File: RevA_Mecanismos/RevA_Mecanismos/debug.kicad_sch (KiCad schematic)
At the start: 2 parts

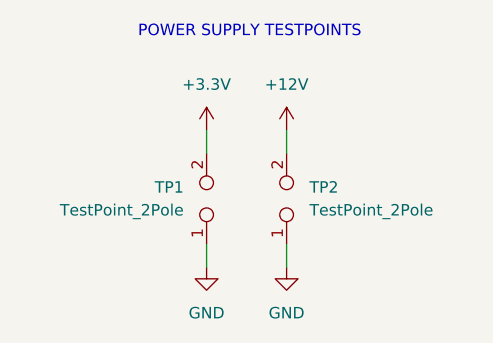
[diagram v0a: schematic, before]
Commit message: Added H-Bridges and voltage regulators
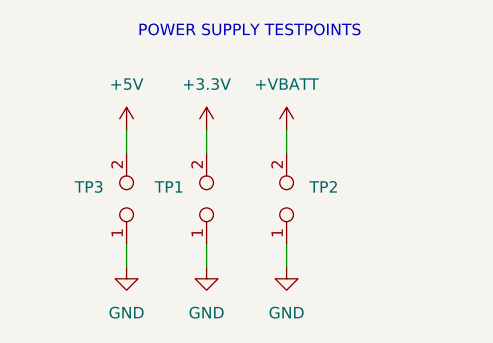
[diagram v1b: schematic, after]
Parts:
- added TP3: TestPoint_2Pole, TestPoint:TestPoint_2Pads_Pitch5.08mm_Drill1.3mm, symbol Connector:TestPoint_2Pole
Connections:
- net GND: now also TP3.1
- net +12V renamed +VMOT
- new net +5V: TP3.2
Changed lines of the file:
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@@
 (kicad_sch (version 20230121) (generator eeschema)
   (paper "A4")
+  (wire (pts (xy 218.44 134.62) (xy 218.44 132.08))
+    (stroke (width 0) (type solid))
+  )
   (wire (pts (xy 236.22 134.62) (xy 236.22 132.08))
     (stroke (width 0) (type default))
@@
     (stroke (width 0) (type solid))
   )
+  (wire (pts (xy 218.44 147.32) (xy 218.44 144.78))
+    (stroke (width 0) (type solid))
+  )
   (wire (pts (xy 236.22 147.32) (xy 236.22 144.78))
     (stroke (width 0) (type solid))
@@
     (effects (font (size 1.27 1.27)) (justify left bottom))
   )
+  (symbol (lib_id "CustomUtilities:+VBATT") (at 236.22 132.08 0) (unit 1)
+    (in_bom yes) (on_board yes) (dnp no)
+    (property "Reference" "#PWR054" (at 236.22 132.08 0)
+      (effects (font (size 1.27 1.27)) hide)
+    )
+    (property "Value" "+VBATT" (at 236.22 127 0)
+      (effects (font (size 1.27 1.27)))
+    )
+    (property "Footprint" "" (at 236.22 132.08 0)
+      (effects (font (size 1.27 1.27)) hide)
+    )
+    (property "Datasheet" "" (at 236.22 132.08 0)
+      (effects (font (size 1.27 1.27)) hide)
+    )
+    (pin "1")
+    (instances
+      (project "RevA_Mecanismos"
+        (path "/3a16a434-10b7-49a8-988b-273362cb395e/9466c5e7-8595-42d4-852d-e47b24624149"
+          (reference "#PWR054") (unit 1)
+        )
+        (path "/3a16a434-10b7-49a8-988b-273362cb395e/a0534dee-4bf0-4ee7-89a4-28a5c95a5477"
+          (reference "#PWR030") (unit 1)
+        )
+      )
+    )
+  )
   (symbol (lib_id "power:GND") (at 227.33 147.32 0) (unit 1)
     (in_bom yes) (on_board yes) (dnp no)
@@
         (path "/6afa037b-8727-4bf3-bca2-b74b900c310e/e4c969ea-19dc-43d6-ab23-93022e90983a"
           (reference "#PWR0170") (unit 1)
+        )
+      )
+    )
+  )
+  (symbol (lib_id "Connector:TestPoint_2Pole") (at 218.44 139.7 90) (unit 1)
+    (in_bom yes) (on_board yes) (dnp no)
+    (property "Reference" "TP3" (at 215.9 138.43 90)
+      (effects (font (size 1.27 1.27)) (justify left))
+    )
+    (property "Value" "TestPoint_2Pole" (at 215.9 140.97 90)
+      (effects (font (size 1.27 1.27)) (justify left) hide)
+    )
+    (property "Footprint" "TestPoint:TestPoint_2Pads_Pitch5.08mm_Drill1.3mm" (at 218.44 139.7 0)
+      (effects (font (size 1.27 1.27)) hide)
+    )
+    (property "Datasheet" "~" (at 218.44 139.7 0)
+      (effects (font (size 1.27 1.27)) hide)
+    )
+    (pin "1")
+    (pin "2")
+    (instances
+      (project "RevA_Mecanismos"
+        (path "/3a16a434-10b7-49a8-988b-273362cb395e/a0534dee-4bf0-4ee7-89a4-28a5c95a5477"
+          (reference "TP3") (unit 1)
+        )
+      )
+      (project "IO_module"
+        (path "/6afa037b-8727-4bf3-bca2-b74b900c310e/e4c969ea-19dc-43d6-ab23-93022e90983a"
+          (reference "TP3") (unit 1)
         )
       )
@@
     )
     (property "Value" "TestPoint_2Pole" (at 238.76 140.97 90)
-      (effects (font (size 1.27 1.27)) (justify right))
+      (effects (font (size 1.27 1.27)) (justify right) hide)
     )
     (property "Footprint" "TestPoint:TestPoint_2Pads_Pitch5.08mm_Drill1.3mm" (at 236.22 139.7 0)
@@
     )
   )
-  (symbol (lib_id "power:+12V") (at 236.22 132.08 0) (unit 1)
-    (in_bom yes) (on_board yes) (dnp no)
-    (property "Reference" "#PWR030" (at 236.22 135.89 0)
-      (effects (font (size 1.27 1.27)) hide)
-    )
-    (property "Value" "+12V" (at 236.22 127 0)
-      (effects (font (size 1.27 1.27)))
-    )
-    (property "Footprint" "" (at 236.22 132.08 0)
-      (effects (font (size 1.27 1.27)) hide)
-    )
-    (property "Datasheet" "" (at 236.22 132.08 0)
-      (effects (font (size 1.27 1.27)) hide)
-    )
-    (pin "1")
-    (instances
-      (project "RevA_Mecanismos"
-        (path "/3a16a434-10b7-49a8-988b-273362cb395e/a0534dee-4bf0-4ee7-89a4-28a5c95a5477"
-          (reference "#PWR030") (unit 1)
-        )
-      )
-      (project "IO_module"
-        (path "/6afa037b-8727-4bf3-bca2-b74b900c310e/e4c969ea-19dc-43d6-ab23-93022e90983a"
-          (reference "#PWR0172") (unit 1)
-        )
-      )
-    )
-  )
   (symbol (lib_id "power:GND") (at 236.22 147.32 0) (unit 1)
     (in_bom yes) (on_board yes) (dnp no)
@@
         (path "/6afa037b-8727-4bf3-bca2-b74b900c310e/e4c969ea-19dc-43d6-ab23-93022e90983a"
           (reference "#PWR0171") (unit 1)
+        )
+      )
+    )
+  )
+  (symbol (lib_id "power:GND") (at 218.44 147.32 0) (unit 1)
+    (in_bom yes) (on_board yes) (dnp no)
+    (property "Reference" "#PWR057" (at 218.44 153.67 0)
+      (effects (font (size 1.27 1.27)) hide)
+    )
+    (property "Value" "GND" (at 218.44 152.4 0)
+      (effects (font (size 1.27 1.27)))
+    )
+    (property "Footprint" "" (at 218.44 147.32 0)
+      (effects (font (size 1.27 1.27)) hide)
+    )
+    (property "Datasheet" "" (at 218.44 147.32 0)
+      (effects (font (size 1.27 1.27)) hide)
+    )
+    (pin "1")
+    (instances
+      (project "RevA_Mecanismos"
+        (path "/3a16a434-10b7-49a8-988b-273362cb395e/a0534dee-4bf0-4ee7-89a4-28a5c95a5477"
+          (reference "#PWR057") (unit 1)
+        )
+      )
+      (project "IO_module"
+        (path "/6afa037b-8727-4bf3-bca2-b74b900c310e/e4c969ea-19dc-43d6-ab23-93022e90983a"
+          (reference "#PWR0170") (unit 1)
+        )
+      )
+    )
+  )
+  (symbol (lib_id "power:+5V") (at 218.44 132.08 0) (unit 1)
+    (in_bom yes) (on_board yes) (dnp no)
+    (property "Reference" "#PWR056" (at 218.44 135.89 0)
+      (effects (font (size 1.27 1.27)) hide)
+    )
+    (property "Value" "+5V" (at 218.44 127 0)
+      (effects (font (size 1.27 1.27)))
+    )
+    (property "Footprint" "" (at 218.44 132.08 0)
+      (effects (font (size 1.27 1.27)) hide)
+    )
+    (property "Datasheet" "" (at 218.44 132.08 0)
+      (effects (font (size 1.27 1.27)) hide)
+    )
+    (pin "1")
+    (instances
+      (project "RevA_Mecanismos"
+        (path "/3a16a434-10b7-49a8-988b-273362cb395e/9466c5e7-8595-42d4-852d-e47b24624149"
+          (reference "#PWR056") (unit 1)
+        )
+        (path "/3a16a434-10b7-49a8-988b-273362cb395e/a0534dee-4bf0-4ee7-89a4-28a5c95a5477"
+          (reference "#PWR055") (unit 1)
+        )
+      )
+      (project "stepper_module_v2"
+        (path "/60aa52ba-7ce7-4ce8-b294-2b47b8740a05/e3d003d9-3702-47a9-9630-ba886331ecbf"
+          (reference "#PWR0141") (unit 1)
         )
       )
@@
     )
     (property "Value" "TestPoint_2Pole" (at 224.79 140.97 90)
-      (effects (font (size 1.27 1.27)) (justify left))
+      (effects (font (size 1.27 1.27)) (justify left) hide)
     )
     (property "Footprint" "TestPoint:TestPoint_2Pads_Pitch5.08mm_Drill1.3mm" (at 227.33 139.7 0)

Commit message: Created PCB project
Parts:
- added D13, D14, D15, D16, D17, D18: LED_Small, LED_SMD:LED_0603_1608Metric, symbol Device:LED_Small
- added J5: DEBUG_CONN, Connector_FFC-FPC:Hirose_FH12-24S-0.5SH_1x24-1MP_P0.50mm_Horizontal, symbol Connector:Conn_01x24_Pin
- added R21, R22, R23, R24, R25, R26: 220, Resistor_SMD:R_0603_1608Metric, symbol Device:R_Small
- added TP4: TestPoint_2Pole, TestPoint:TestPoint_2Pads_Pitch5.08mm_Drill1.3mm, symbol Connector:TestPoint_2Pole
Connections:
- net +3.3V: now also J5.24 (Pin_24)
- net GND: now also J5.22 (Pin_22), J5.23 (Pin_23), R21.2, R22.2, R23.2, R24.2, R25.2, R26.2
- new net: D18.1 (K), R26.1
- new net: D14.1 (K), R22.1
- new net: D17.1 (K), R25.1
- new net: D15.1 (K), R23.1
- new net: D13.1 (K), R21.1
- new net: D16.1 (K), R24.1
- new net CAN_RX: J5.18 (Pin_18), TP4.1
- new net CAN_TX: J5.19 (Pin_19), TP4.2
- new net DEBUG_1: D13.2 (A), J5.1 (Pin_1)
- new net DEBUG_2: D14.2 (A), J5.2 (Pin_2)
- new net DEBUG_3: D15.2 (A), J5.3 (Pin_3)
- new net DEBUG_4: D16.2 (A), J5.4 (Pin_4)
- new net DEBUG_5: D17.2 (A), J5.5 (Pin_5)
- new net DEBUG_6: D18.2 (A), J5.6 (Pin_6)
- new net SCL: J5.15 (Pin_15)
- new net SDA: J5.14 (Pin_14)
- new net UART_RX: J5.21 (Pin_21)
- new net UART_TX: J5.20 (Pin_20)
- no-connect marks 0 -> 9
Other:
- note added: "CANBUS TESTPOINTS"
- note added: "DEBUG CONNECTOR"
- note added: "DEBUG LEDS"
- note added: "Debug"
- note added: "FH12-24S-0.5SH(55)"

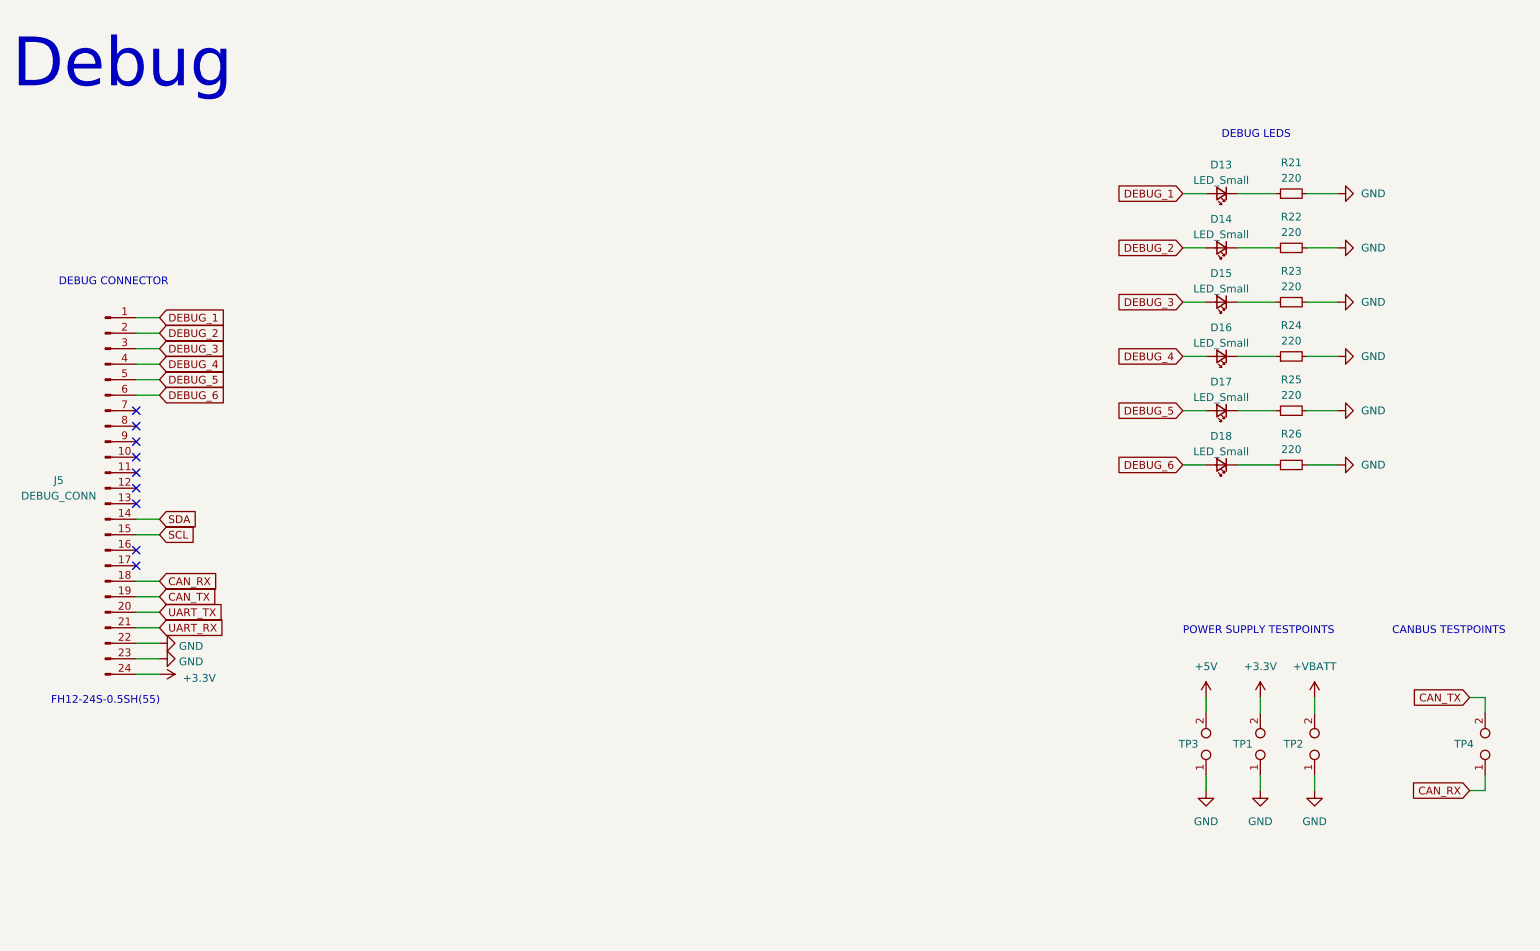
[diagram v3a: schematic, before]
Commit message: Updated STM32 USV Mechanism PCB
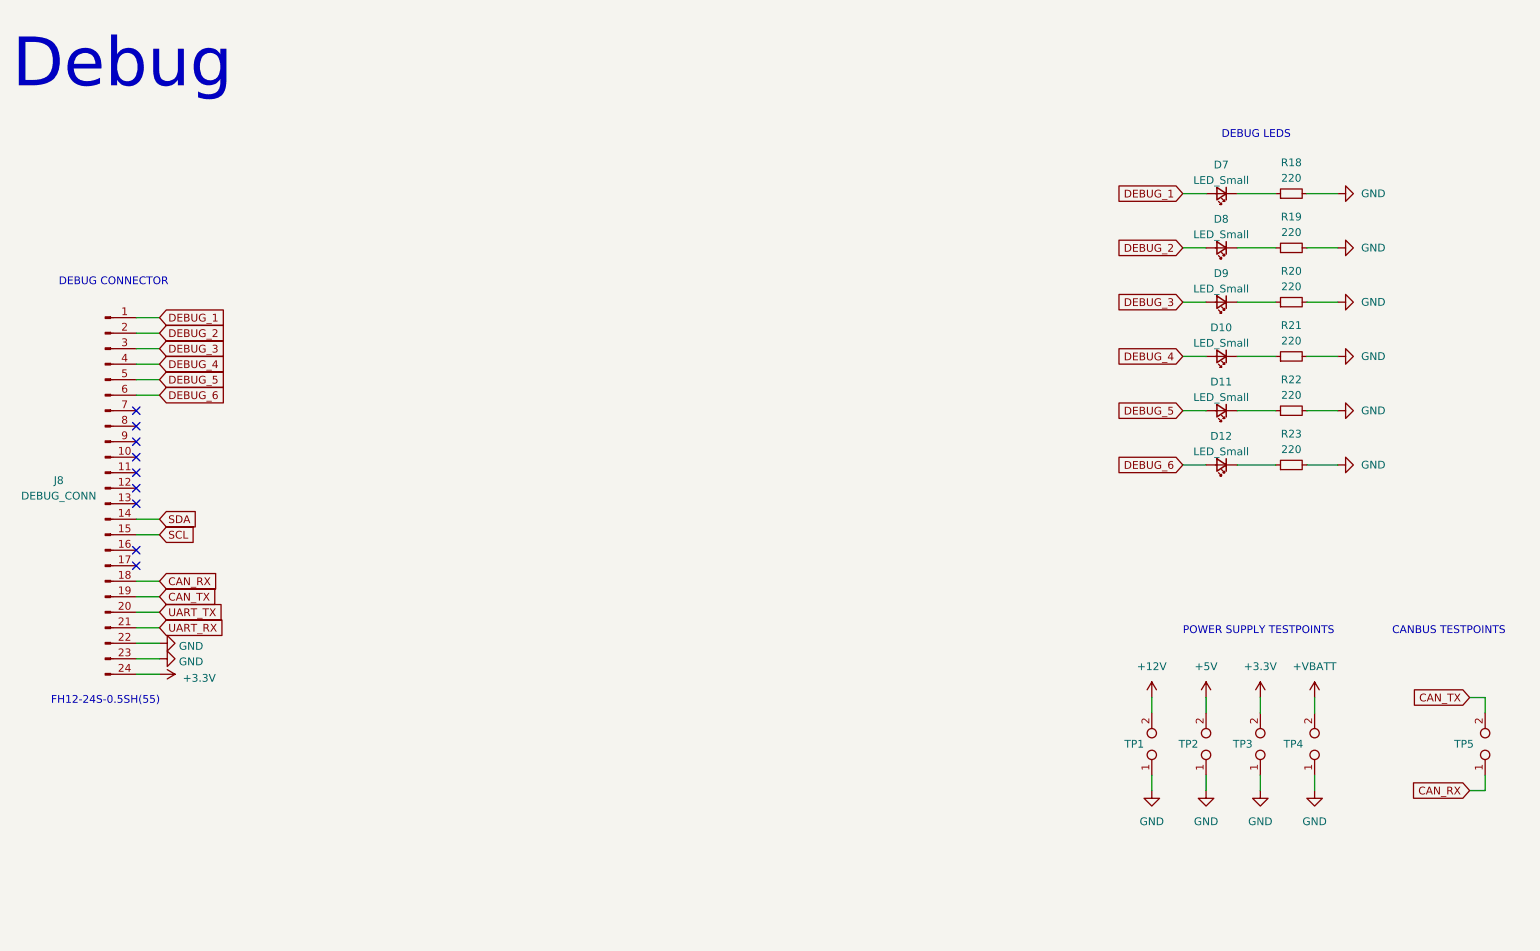
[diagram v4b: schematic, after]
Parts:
- added TP1: TestPoint_2Pole, TestPoint:TestPoint_2Pads_Pitch5.08mm_Drill1.3mm, symbol Connector:TestPoint_2Pole
- renumbered D16 to D10, D17 to D11, D18 to D12, D13 to D7, D14 to D8, D15 to D9, J5 to J8, R21 to R18, R22 to R19, R23 to R20, R24 to R21, R25 to R22, R26 to R23, TP3 to TP2, TP1 to TP3, TP2 to TP4, TP4 to TP5
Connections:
- net GND: now also TP1.1
- new net +12V: TP1.2

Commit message: Complete schematic and pcb designs, routes missing and not yet complete
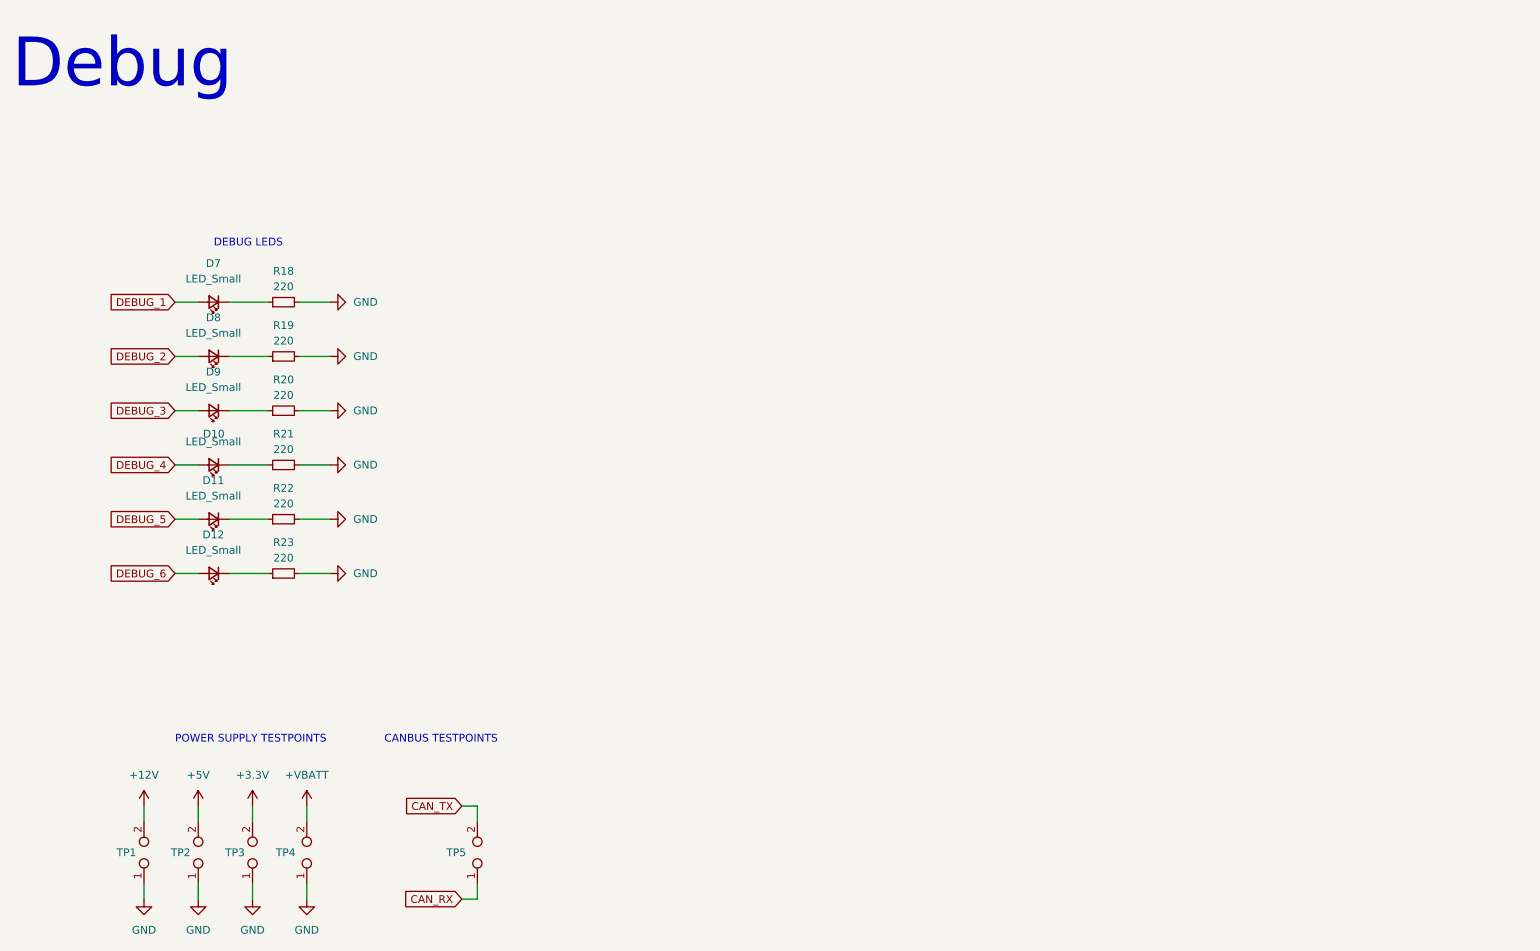
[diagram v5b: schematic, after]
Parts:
- removed J8: DEBUG_CONN, Connector_FFC-FPC:Hirose_FH12-24S-0.5SH_1x24-1MP_P0.50mm_Horizontal, symbol Connector:Conn_01x24_Pin
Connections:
- no-connect marks 9 -> 0
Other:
- note removed: "DEBUG CONNECTOR"
- note removed: "FH12-24S-0.5SH(55)"
- moved on the sheet: D10, D11, D12, D7, D8, D9, R18, R19, R20, R21, R22, R23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
